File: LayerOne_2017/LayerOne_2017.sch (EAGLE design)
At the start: 107 parts, among them IC1 STM32F446_LQFP64LQFP64, IC2 REG1117, J1 SPI_TFT_DISPLAY, Q1 2N2222, Q2 MMBT2222A, U1 SN65HVD235DR, U2 SN65HVD235DR, U4 SDCARD, U5 FERRITE0805, U6 LM2621MM, X1 STEREOJACK, X2 MINI-USB-32005-301

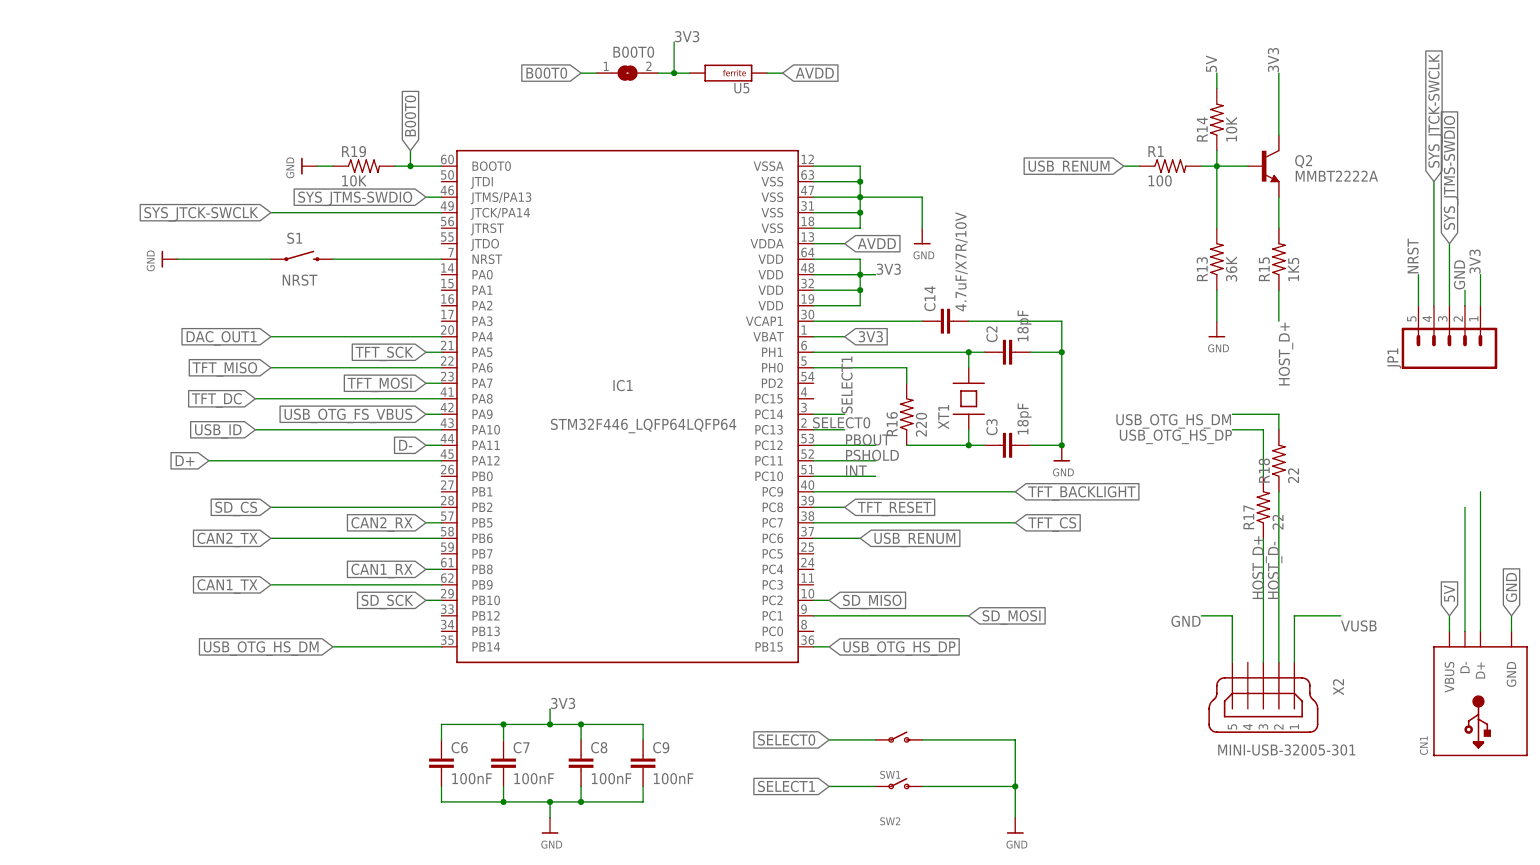
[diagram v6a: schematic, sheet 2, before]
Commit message: xmas update! added leds added caps to d+/d- fixed led backlight added cap to vreg
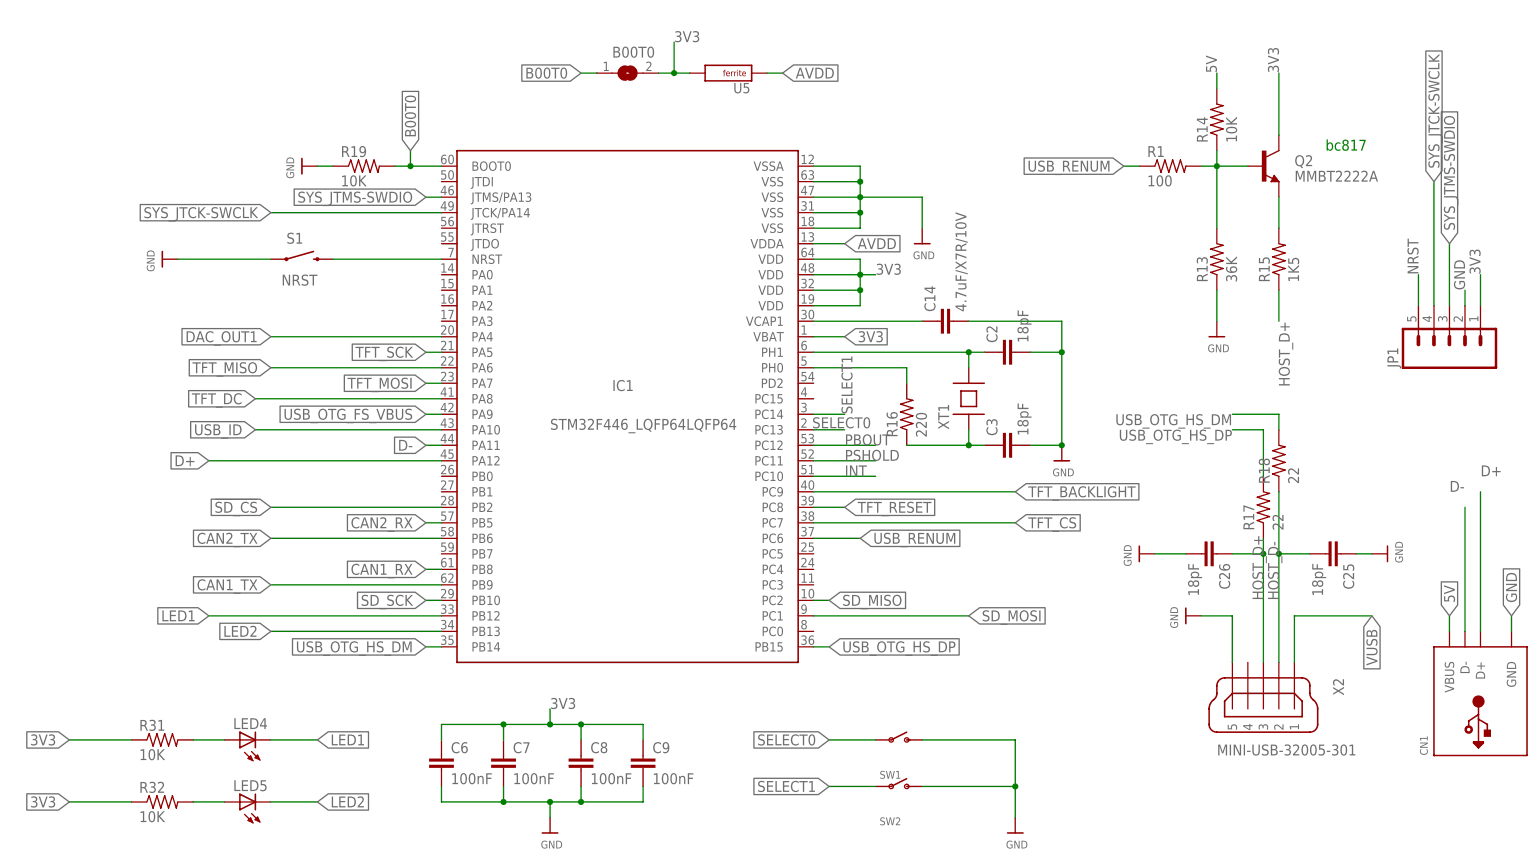
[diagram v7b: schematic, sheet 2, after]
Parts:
- added C24: 0.1uF, SparkFun-Passives:CAP0805
- added C25, C26: 18pF, SparkFun-Passives:CAP0805
- added LED4, LED5: (no value), led:LEDCHIP-LED0805
- added R31, R32: 10K, SparkFun-Passives:RESISTOR0805-RES
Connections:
- removed net TFT_LCD: J1.LED, Q1.C, U3.LEDK@1, U3.LEDK@2, U3.LEDK@3, U3.LEDK@4
- new net LCD_BACKLIGHT_LOW: Q1.C, U3.LEDK@1, U3.LEDK@2, U3.LEDK@3, U3.LEDK@4
- new net LED1: IC1.PB12, LED4.C
- new net LED2: IC1.PB13, LED5.C
- new net N$38: LED4.A, R31.2
- new net N$39: LED5.A, R32.2
- net 3V3: now also C24.1, R31.1, R32.1
- net GND: now also C24.2, C25.1, C26.2
- net HOST_D+: now also C26.1
- net HOST_D-: now also C25.2
- net TFT_BACKLIGHT: now also J1.LED
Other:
- note added: "bc817"
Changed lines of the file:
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@@
 <part name="3V3" library="testpad" deviceset="PTR1" device="PAD1-13"/>
 <part name="U6" library="LM2621MM" deviceset="LM2621MM" device=""/>
+<part name="C24" library="SparkFun-Passives" deviceset="CAP" device="0805" value="0.1uF"/>
+<part name="U$21" library="microbuilder" deviceset="GND" device=""/>
+<part name="C25" library="SparkFun-Passives" deviceset="CAP" device="0805" value="18pF"/>
+<part name="C26" library="SparkFun-Passives" deviceset="CAP" device="0805" value="18pF"/>
+<part name="U$30" library="microbuilder" deviceset="GND" device=""/>
+<part name="U$44" library="microbuilder" deviceset="GND" device=""/>
+<part name="U$45" library="microbuilder" deviceset="GND" device=""/>
+<part name="LED4" library="led" deviceset="LED" device="CHIP-LED0805"/>
+<part name="LED5" library="led" deviceset="LED" device="CHIP-LED0805"/>
+<part name="R31" library="SparkFun-Passives" deviceset="RESISTOR" device="0805-RES" value="10K"/>
+<part name="R32" library="SparkFun-Passives" deviceset="RESISTOR" device="0805-RES" value="10K"/>
 </parts>
 <sheets>
@@
 <instance part="FID3" gate="G$1" x="-116.84" y="101.6"/>
 <instance part="3V3" gate="G$1" x="-88.9" y="101.6" rot="R180"/>
+<instance part="C24" gate="G$1" x="-73.66" y="78.74"/>
+<instance part="U$21" gate="G$1" x="-73.66" y="71.12"/>
 </instances>
 <busses>
@@
 <pinref part="U$12" gate="G$1" pin="GND"/>
 </segment>
+<segment>
+<pinref part="C24" gate="G$1" pin="2"/>
+<pinref part="U$21" gate="G$1" pin="GND"/>
+<wire x1="-73.66" y1="73.66" x2="-73.66" y2="76.2" width="0.1524" layer="91"/>
+</segment>
 </net>
 <net name="3V3" class="0">
 <segment>
-<label x="-81.28" y="88.9" size="1.778" layer="95" xref="yes"/>
+<label x="-68.58" y="88.9" size="1.778" layer="95" xref="yes"/>
 <pinref part="IC2" gate="G$1" pin="VOUT"/>
 <wire x1="-93.98" y1="88.9" x2="-88.9" y2="88.9" width="0.1524" layer="91"/>
-<wire x1="-88.9" y1="88.9" x2="-83.82" y2="88.9" width="0.1524" layer="91"/>
 <pinref part="C5" gate="G$1" pin="1"/>
 <wire x1="-88.9" y1="88.9" x2="-88.9" y2="83.82" width="0.1524" layer="91"/>
 <junction x="-88.9" y="88.9"/>
-<wire x1="-83.82" y1="88.9" x2="-81.28" y2="88.9" width="0.1524" layer="91"/>
+<wire x1="-88.9" y1="88.9" x2="-73.66" y2="88.9" width="0.1524" layer="91"/>
 <pinref part="3V3" gate="G$1" pin="TP"/>
+<wire x1="-73.66" y1="88.9" x2="-68.58" y2="88.9" width="0.1524" layer="91"/>
 <wire x1="-88.9" y1="88.9" x2="-88.9" y2="99.06" width="0.1524" layer="91"/>
+<pinref part="C24" gate="G$1" pin="1"/>
+<wire x1="-73.66" y1="88.9" x2="-73.66" y2="83.82" width="0.1524" layer="91"/>
+<junction x="-73.66" y="88.9"/>
 </segment>
 </net>
@@
 <sheet>
 <plain>
+<text x="185.42" y="121.92" size="1.778" layer="91">bc817</text>
 </plain>
 <instances>
@@
 <instance part="S1" gate="G$1" x="17.78" y="104.14"/>
 <instance part="U$20" gate="G$1" x="-5.08" y="104.14" rot="R270"/>
+<instance part="C25" gate="G$1" x="185.42" y="55.88" rot="R270"/>
+<instance part="C26" gate="G$1" x="165.1" y="55.88" rot="R270"/>
+<instance part="U$30" gate="G$1" x="162.56" y="45.72" rot="R270"/>
+<instance part="U$44" gate="G$1" x="154.94" y="55.88" rot="R270"/>
+<instance part="U$45" gate="G$1" x="195.58" y="55.88" rot="R90"/>
+<instance part="LED4" gate="G$1" x="7.62" y="25.4" rot="R90"/>
+<instance part="LED5" gate="G$1" x="7.62" y="15.24" rot="R90"/>
+<instance part="R31" gate="G$1" x="-5.08" y="25.4"/>
+<instance part="R32" gate="G$1" x="-5.08" y="15.24"/>
 </instances>
 <busses>
@@
 <wire x1="170.18" y1="38.1" x2="170.18" y2="45.72" width="0.1524" layer="91"/>
 <wire x1="170.18" y1="45.72" x2="165.1" y2="45.72" width="0.1524" layer="91"/>
-<label x="165.1" y="45.72" size="1.778" layer="95" rot="R180"/>
+<pinref part="U$30" gate="G$1" pin="GND"/>
 </segment>
 <segment>
@@
 <wire x1="-2.54" y1="104.14" x2="12.7" y2="104.14" width="0.1524" layer="91"/>
 </segment>
+<segment>
+<pinref part="C25" gate="G$1" pin="1"/>
+<pinref part="U$45" gate="G$1" pin="GND"/>
+<wire x1="193.04" y1="55.88" x2="190.5" y2="55.88" width="0.1524" layer="91"/>
+</segment>
+<segment>
+<pinref part="C26" gate="G$1" pin="2"/>
+<pinref part="U$44" gate="G$1" pin="GND"/>
+<wire x1="157.48" y1="55.88" x2="162.56" y2="55.88" width="0.1524" layer="91"/>
+</segment>
 </net>
 <net name="3V3" class="0">
@@
 <label x="106.68" y="91.44" size="1.778" layer="95" xref="yes"/>
 </segment>
+<segment>
+<pinref part="R31" gate="G$1" pin="1"/>
+<wire x1="-10.16" y1="25.4" x2="-20.32" y2="25.4" width="0.1524" layer="91"/>
+<label x="-20.32" y="25.4" size="1.778" layer="95" rot="R180" xref="yes"/>
+</segment>
+<segment>
+<pinref part="R32" gate="G$1" pin="1"/>
+<wire x1="-10.16" y1="15.24" x2="-20.32" y2="15.24" width="0.1524" layer="91"/>
+<label x="-20.32" y="15.24" size="1.778" layer="95" rot="R180" xref="yes"/>
+</segment>
 </net>
 <net name="N$10" class="0">
@@
 <pinref part="CN1" gate="G$1" pin="D-"/>
 <wire x1="208.28" y1="43.18" x2="208.28" y2="63.5" width="0.1524" layer="91"/>
+<label x="205.74" y="66.04" size="1.778" layer="95"/>
 </segment>
 </net>
@@
 <pinref part="CN1" gate="G$1" pin="D+"/>
 <wire x1="210.82" y1="43.18" x2="210.82" y2="66.04" width="0.1524" layer="91"/>
+<label x="210.82" y="68.58" size="1.778" layer="95"/>
 </segment>
 </net>
@@
 <segment>
 <pinref part="X2" gate="G$1" pin="3"/>
-<wire x1="175.26" y1="38.1" x2="175.26" y2="58.42" width="0.1524" layer="91"/>
+<wire x1="175.26" y1="38.1" x2="175.26" y2="55.88" width="0.1524" layer="91"/>
 <label x="175.26" y="48.26" size="1.778" layer="95" rot="R90"/>
 <pinref part="R17" gate="G$1" pin="1"/>
+<pinref part="C26" gate="G$1" pin="1"/>
+<wire x1="175.26" y1="55.88" x2="175.26" y2="58.42" width="0.1524" layer="91"/>
+<wire x1="175.26" y1="55.88" x2="170.18" y2="55.88" width="0.1524" layer="91"/>
+<junction x="175.26" y="55.88"/>
 </segment>
 <segment>
@@
 <label x="177.8" y="48.26" size="1.778" layer="95" rot="R90"/>
 <pinref part="R18" gate="G$1" pin="1"/>
-<wire x1="177.8" y1="38.1" x2="177.8" y2="66.04" width="0.1524" layer="91"/>
+<wire x1="177.8" y1="38.1" x2="177.8" y2="55.88" width="0.1524" layer="91"/>
+<pinref part="C25" gate="G$1" pin="2"/>
+<wire x1="177.8" y1="55.88" x2="177.8" y2="66.04" width="0.1524" layer="91"/>
+<wire x1="177.8" y1="55.88" x2="182.88" y2="55.88" width="0.1524" layer="91"/>
+<junction x="177.8" y="55.88"/>
 </segment>
 </net>
@@
 <segment>
 <pinref part="IC1" gate="G$1" pin="PB14"/>
-<wire x1="40.64" y1="40.64" x2="22.86" y2="40.64" width="0.1524" layer="91"/>
-<label x="22.86" y="40.64" size="1.778" layer="95" rot="R180" xref="yes"/>
+<wire x1="40.64" y1="40.64" x2="38.1" y2="40.64" width="0.1524" layer="91"/>
+<label x="38.1" y="40.64" size="1.778" layer="95" rot="R180" xref="yes"/>
 </segment>
 </net>
@@
 <pinref part="X2" gate="G$1" pin="1"/>
 <wire x1="180.34" y1="38.1" x2="180.34" y2="45.72" width="0.1524" layer="91"/>
-<wire x1="180.34" y1="45.72" x2="187.96" y2="45.72" width="0.1524" layer="91"/>
-<label x="187.96" y="43.18" size="1.778" layer="95"/>
+<wire x1="180.34" y1="45.72" x2="193.04" y2="45.72" width="0.1524" layer="91"/>
+<label x="193.04" y="45.72" size="1.778" layer="95" rot="R270" xref="yes"/>
 </segment>
 </net>
@@
 <wire x1="101.6" y1="68.58" x2="111.76" y2="68.58" width="0.1524" layer="91"/>
 <label x="106.68" y="68.58" size="1.778" layer="95"/>
+</segment>
+</net>
+<net name="N$38" class="0">
+<segment>
+<pinref part="LED4" gate="G$1" pin="A"/>
+<pinref part="R31" gate="G$1" pin="2"/>
+<wire x1="5.08" y1="25.4" x2="0" y2="25.4" width="0.1524" layer="91"/>
+</segment>
+</net>
+<net name="N$39" class="0">
+<segment>
+<pinref part="R32" gate="G$1" pin="2"/>
+<pinref part="LED5" gate="G$1" pin="A"/>
+<wire x1="0" y1="15.24" x2="5.08" y2="15.24" width="0.1524" layer="91"/>
+</segment>
+</net>
+<net name="LED1" class="0">
+<segment>
+<pinref part="LED4" gate="G$1" pin="C"/>
+<wire x1="12.7" y1="25.4" x2="20.32" y2="25.4" width="0.1524" layer="91"/>
+<label x="20.32" y="25.4" size="1.778" layer="95" xref="yes"/>
+</segment>
+<segment>
+<pinref part="IC1" gate="G$1" pin="PB12"/>
+<wire x1="40.64" y1="45.72" x2="2.54" y2="45.72" width="0.1524" layer="91"/>
+<label x="2.54" y="45.72" size="1.778" layer="95" rot="R180" xref="yes"/>
+</segment>
+</net>
+<net name="LED2" class="0">
+<segment>
+<pinref part="LED5" gate="G$1" pin="C"/>
+<wire x1="12.7" y1="15.24" x2="20.32" y2="15.24" width="0.1524" layer="91"/>
+<label x="20.32" y="15.24" size="1.778" layer="95" xref="yes"/>
+</segment>
+<segment>
+<pinref part="IC1" gate="G$1" pin="PB13"/>
+<wire x1="40.64" y1="43.18" x2="12.7" y2="43.18" width="0.1524" layer="91"/>
+<label x="12.7" y="43.18" size="1.778" layer="95" rot="R180" xref="yes"/>
 </segment>
 </net>
@@
 </segment>
 </net>
-<net name="TFT_LCD" class="0">
+<net name="LCD_BACKLIGHT_LOW" class="0">
 <segment>
 <wire x1="50.8" y1="33.02" x2="50.8" y2="30.48" width="0.1524" layer="91"/>
@@
 <junction x="86.36" y="27.94"/>
 </segment>
-<segment>
-<label x="76.2" y="81.28" size="1.778" layer="95" rot="R180" xref="yes"/>
-<pinref part="J1" gate="G$1" pin="LED"/>
-<wire x1="111.76" y1="81.28" x2="76.2" y2="81.28" width="0.1524" layer="91"/>
-</segment>
 </net>
 <net name="N$16" class="0">
@@
 <pinref part="R10" gate="G$1" pin="1"/>
 </segment>
-</net>
+<segment>
+<pinref part="J1" gate="G$1" pin="LED"/>
+<wire x1="111.76" y1="81.28" x2="83.82" y2="81.28" width="0.1524" layer="91"/>
+<label x="83.82" y="81.28" size="1.778" layer="95" rot="R180" xref="yes"/>
+</segment>
+</net>
